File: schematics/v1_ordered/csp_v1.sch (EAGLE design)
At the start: 71 parts, among them IC1 74AHC1G08DCK, IC2 74HCT04D, IC3 PCA9555PW, J1 2X20-CHIP2X20-SMT-CHIP, U2 DS2431P

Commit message: optimized schematic to one page
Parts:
- removed L_BUTTONS: FH12-10S-0.5SH, con-hirose:FH12-10S-0.5SH
- removed R_BUTTONS: FH12-24S-0.5SH, con-hirose:FH12-24S-0.5SH
- added L_B: FH12-10S-0.5SH, con-hirose:FH12-10S-0.5SH
- added R_B: FH12-24S-0.5SH, con-hirose:FH12-24S-0.5SH
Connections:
- net !CHARGE_LED: now also R_B-14.1; no longer R_BUTTONS-14.1
- net !POWER_LED: now also R_B-16.1; no longer R_BUTTONS-16.1
- net CIRCLE: now also R_B-20.1; no longer R_BUTTONS-20.1
- net DISPLAY: now also R_B-5.1; no longer R_BUTTONS-5.1
- net DOWN: now also L_B-3.1; no longer L_BUTTONS-3.1
- net GND: now also L_B-1.1, L_B-5.1, L_B-6.1, L_B-7.1, L_B-9.1, R_B-1.1, R_B-10.1, R_B-11.1, R_B-15.1, R_B-21.1, R_B-23.1, R_B-9.1; no longer L_BUTTONS-1.1, L_BUTTONS-5.1, L_BUTTONS-6.1, L_BUTTONS-7.1, L_BUTTONS-9.1, R_BUTTONS-1.1, R_BUTTONS-10.1, R_BUTTONS-11.1, R_BUTTONS-15.1, R_BUTTONS-21.1, R_BUTTONS-23.1, R_BUTTONS-9.1
- net HOME: now also R_B-2.1; no longer R_BUTTONS-2.1
- net LEFT: now also L_B-8.1; no longer L_BUTTONS-8.1
- net L_TRIGGER: now also L_B-10.1; no longer L_BUTTONS-10.1
- net MUTE: now also R_B-6.1; no longer R_BUTTONS-6.1
- net PWR_ON: now also R_B-12.1; no longer R_BUTTONS-12.1
- net RIGHT: now also L_B-2.1; no longer L_BUTTONS-2.1
- net R_TRIGGER: now also R_B-24.1; no longer R_BUTTONS-24.1
- net SELECT: now also R_B-7.1; no longer R_BUTTONS-7.1
- net SQUARE: now also R_B-18.1; no longer R_BUTTONS-18.1
- net START: now also R_B-8.1; no longer R_BUTTONS-8.1
- net SWITCH_4: now also R_B-13.1; no longer R_BUTTONS-13.1
- net TRIANGE: now also R_B-19.1; no longer R_BUTTONS-19.1
- net UP: now also L_B-4.1; no longer L_BUTTONS-4.1
- net VCC5V: now also R_B-22.1; no longer R_BUTTONS-22.1
- net VOL+: now also R_B-4.1; no longer R_BUTTONS-4.1
- net VOL-: now also R_B-3.1; no longer R_BUTTONS-3.1
- net X: now also R_B-17.1; no longer R_BUTTONS-17.1
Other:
- note added: "1wire"
- note added: "Display"
- note added: "GPIO extender"
- note added: "SD card"
- note added: "inverter"
- note removed: "1W EEPROM"
- note removed: "<- cut here"
- note removed: "BLUE"
- note removed: "GREEN"
- note removed: "RED"
- note removed: "cut here"
- moved on the sheet: BAT, C1, C10, C11, C12, C13, C14, C15, C16, C2, C3, C4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

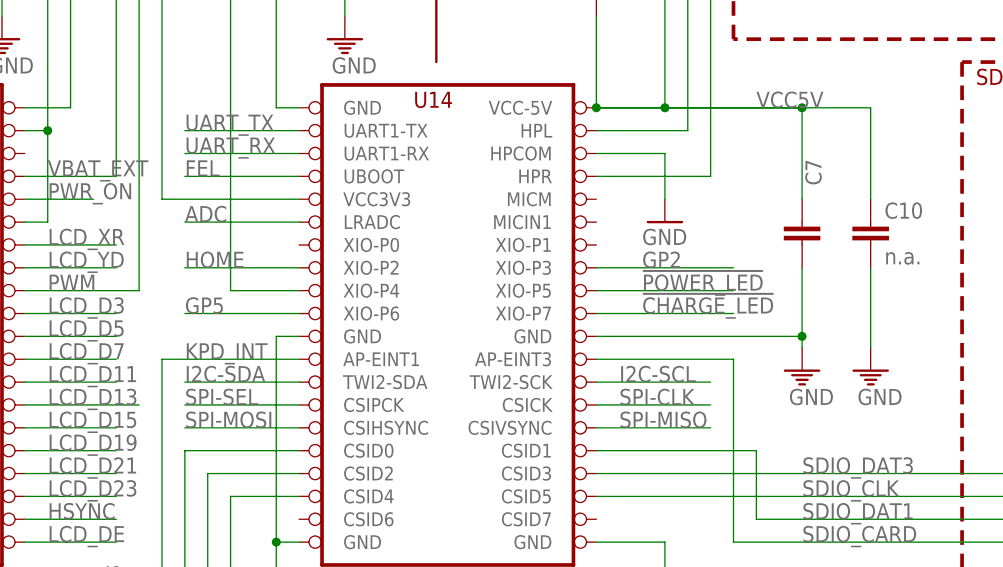
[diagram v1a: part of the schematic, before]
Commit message: flip p5 to p6 in schematic, to account for bug, no layout change
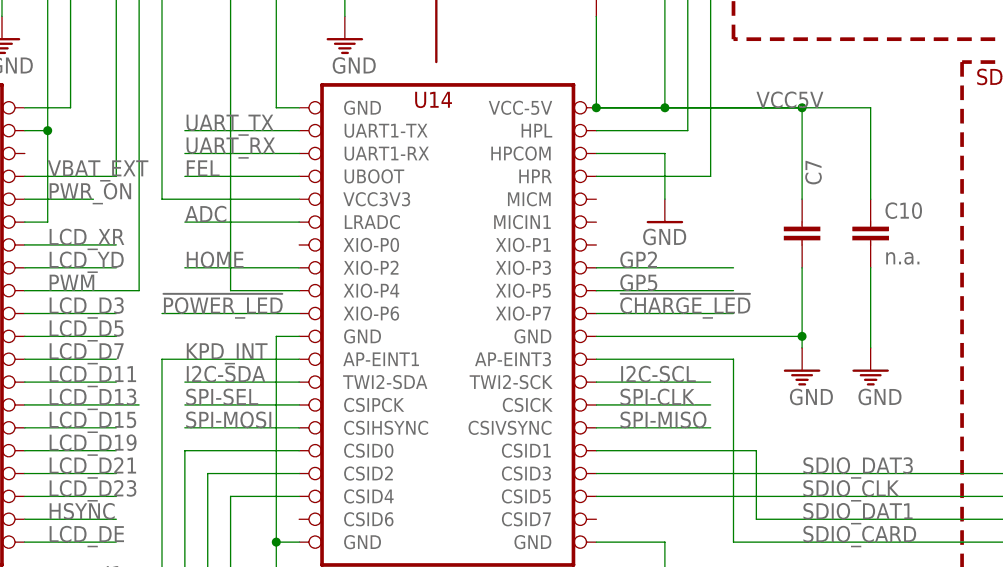
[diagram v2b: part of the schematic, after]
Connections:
- net !POWER_LED: now also J1.XIO-P6; no longer J1.XIO-P5
- net GP5: now also J1.XIO-P5; no longer J1.XIO-P6
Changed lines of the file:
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@@
 <?xml version="1.0" encoding="utf-8"?>
 <!DOCTYPE eagle SYSTEM "eagle.dtd">
-<eagle version="7.7.0">
+<eagle version="7.6.0">
 <drawing>
 <settings>
@@
 <segment>
 <wire x1="500.38" y1="152.4" x2="515.62" y2="152.4" width="0.1524" layer="91"/>
-<label x="505.46" y="152.4" size="1.778" layer="95" font="vector" ratio="12"/>
+<label x="502.92" y="152.4" size="1.778" layer="95" font="vector" ratio="12"/>
 <pinref part="J1" gate="G$1" pin="XIO-P3"/>
 </segment>
@@
 <junction x="312.42" y="246.38"/>
 <label x="426.72" y="203.2" size="1.778" layer="95"/>
-</segment>
-</net>
-<net name="GP5" class="0">
-<segment>
-<wire x1="467.36" y1="147.32" x2="454.66" y2="147.32" width="0.1524" layer="91"/>
-<label x="454.66" y="147.32" size="1.778" layer="95" font="vector" ratio="12"/>
-<pinref part="J1" gate="G$1" pin="XIO-P6"/>
 </segment>
 </net>
@@
 </segment>
 <segment>
-<wire x1="500.38" y1="149.86" x2="515.62" y2="149.86" width="0.1524" layer="91"/>
-<label x="505.46" y="149.86" size="1.778" layer="95" font="vector" ratio="12"/>
-<pinref part="J1" gate="G$1" pin="XIO-P5"/>
+<wire x1="467.36" y1="147.32" x2="452.12" y2="147.32" width="0.1524" layer="91"/>
+<label x="452.12" y="147.32" size="1.778" layer="95" font="vector" ratio="12"/>
+<pinref part="J1" gate="G$1" pin="XIO-P6"/>
 </segment>
 </net>
@@
 <segment>
 <wire x1="500.38" y1="147.32" x2="515.62" y2="147.32" width="0.1524" layer="91"/>
-<label x="505.46" y="147.32" size="1.778" layer="95" font="vector" ratio="12"/>
+<label x="502.92" y="147.32" size="1.778" layer="95" font="vector" ratio="12"/>
 <pinref part="J1" gate="G$1" pin="XIO-P7"/>
 </segment>
@@
 </segment>
 </net>
+<net name="GP5" class="0">
+<segment>
+<wire x1="500.38" y1="149.86" x2="515.62" y2="149.86" width="0.1524" layer="91"/>
+<label x="502.92" y="149.86" size="1.778" layer="95" font="vector" ratio="12"/>
+<pinref part="J1" gate="G$1" pin="XIO-P5"/>
+</segment>
+</net>
